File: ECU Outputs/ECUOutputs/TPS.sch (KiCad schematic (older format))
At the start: 22 parts, among them Q6 Q_NPN_BCE, Q7 Q_NPN_BCE, Q8 Q_PNP_BCE

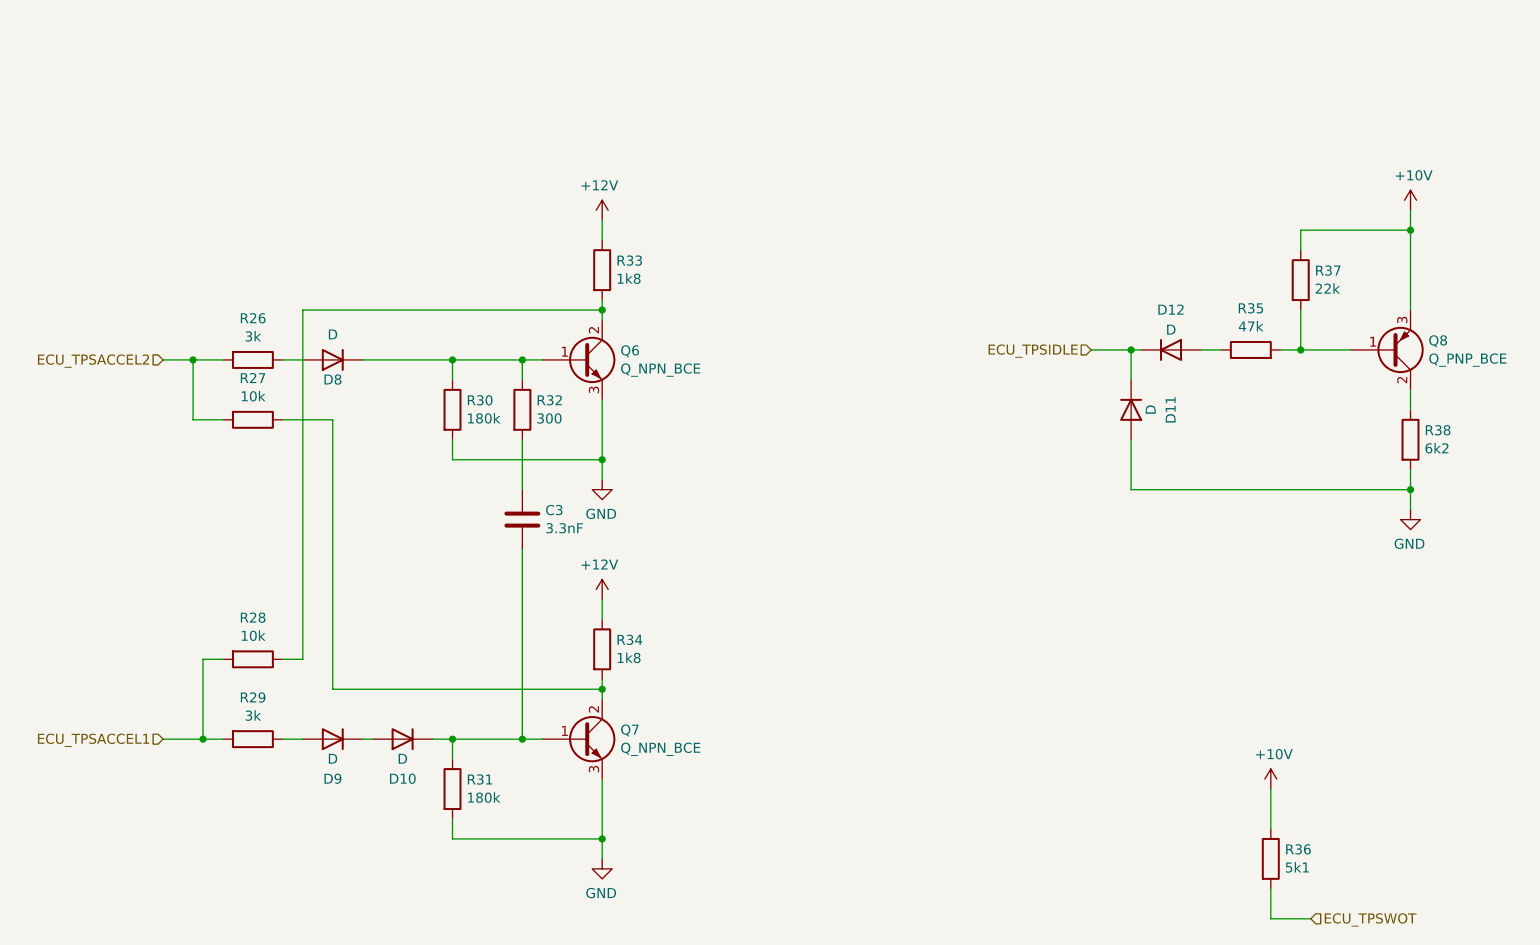
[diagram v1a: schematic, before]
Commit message: Updated manufacturer part numbers. Working on ECU outputs tester board.
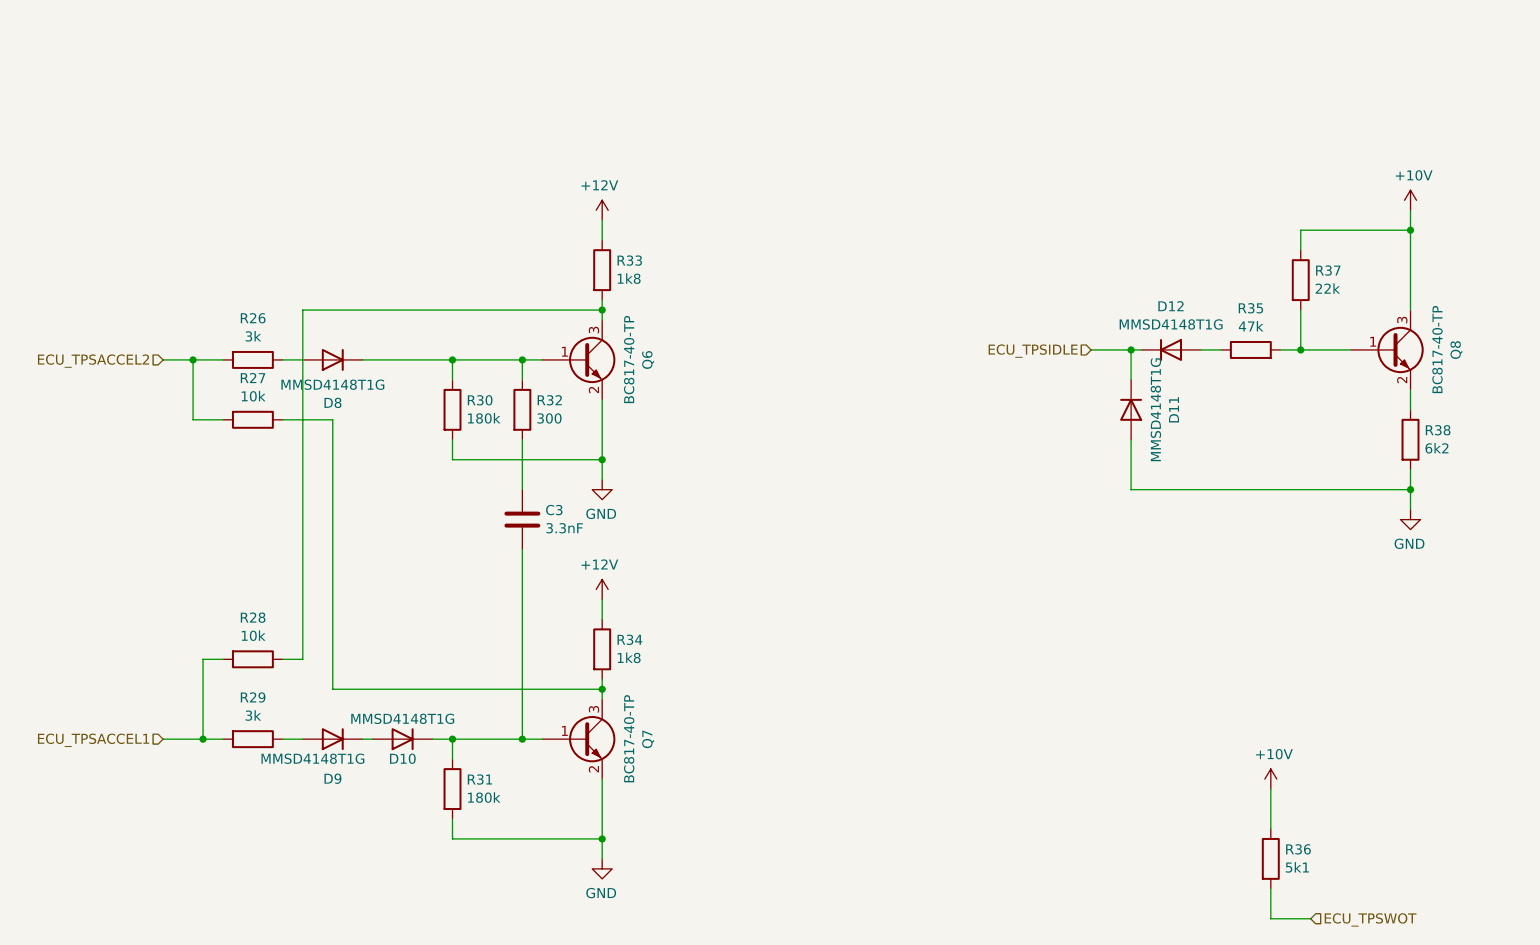
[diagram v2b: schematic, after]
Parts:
- removed Q6, Q7: Q_NPN_BCE, symbol Device:Q_NPN_BCE
- removed Q8: Q_PNP_BCE, symbol Device:Q_PNP_BCE
- added Q6, Q7, Q8: BC817-40-TP, Package_TO_SOT_SMD:SOT-23, symbol Device:Q_NPN_BEC
- C3: footprint (none) -> Capacitor_SMD:C_0805_2012Metric
- D10, D11, D12, D8, D9: value D -> MMSD4148T1G; footprint (none) -> Diode_SMD:D_SOD-123; manf# (none) -> MMSD4148T1G
- R26, R27, R28, R29, R30, R31, R32, R33, R34, R35, R36, R37, R38: footprint (none) -> Resistor_SMD:R_0805_2012Metric
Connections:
- net +10V: now also Q8.3 (C)
- net GND: now also Q6.2 (E), Q7.2 (E)
- net at R28.1, R33.2: now also Q6.3 (C)
- net at D8.1 (K), R30.1, R32.1: now also Q6.1 (B)
- net at R27.1, R34.2: now also Q7.3 (C)
- net at C3.2, D10.1 (K), R31.1: now also Q7.1 (B)
- net at R35.2, R37.2: now also Q8.1 (B)
- net at R38.1: now also Q8.2 (E)
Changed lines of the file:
@@
 F 0 "R33" H 4820 2396 50  0000 L CNN
 F 1 "1k8" H 4820 2305 50  0000 L CNN
-F 2 "" V 4680 2350 50  0001 C CNN
+F 2 "Resistor_SMD:R_0805_2012Metric" V 4680 2350 50  0001 C CNN
 F 3 "~" H 4750 2350 50  0001 C CNN
 	1    4750 2350
-	1    0    0    -1
-$EndComp
-$Comp
-L Device:Q_NPN_BCE Q?
-U 1 1 604AAF04
-P 4650 2800
-AR Path="/60469408/604AAF04" Ref="Q?"  Part="1"
-AR Path="/604A55C0/604AAF04" Ref="Q6"  Part="1"
-F 0 "Q6" H 4841 2846 50  0000 L CNN
-F 1 "Q_NPN_BCE" H 4841 2755 50  0000 L CNN
-F 2 "" H 4850 2900 50  0001 C CNN
-F 3 "~" H 4650 2800 50  0001 C CNN
-	1    4650 2800
 	1    0    0    -1
 $EndComp
@@
 F 0 "R30" H 4070 3096 50  0000 L CNN
 F 1 "180k" H 4070 3005 50  0000 L CNN
-F 2 "" V 3930 3050 50  0001 C CNN
+F 2 "Resistor_SMD:R_0805_2012Metric" V 3930 3050 50  0001 C CNN
 F 3 "~" H 4000 3050 50  0001 C CNN
 	1    4000 3050
@@
 F 0 "R32" H 4420 3096 50  0000 L CNN
 F 1 "300" H 4420 3005 50  0000 L CNN
-F 2 "" V 4280 3050 50  0001 C CNN
+F 2 "Resistor_SMD:R_0805_2012Metric" V 4280 3050 50  0001 C CNN
 F 3 "~" H 4350 3050 50  0001 C CNN
 	1    4350 3050
@@
 $EndComp
 Connection ~ 4000 2800
-$Comp
-L Device:D D?
-U 1 1 604AAF22
-P 3400 2800
-AR Path="/60469408/604AAF22" Ref="D?"  Part="1"
-AR Path="/604A55C0/604AAF22" Ref="D8"  Part="1"
-F 0 "D8" H 3400 2900 50  0000 C CNN
-F 1 "D" H 3400 2674 50  0000 C CNN
-F 2 "" H 3400 2800 50  0001 C CNN
-F 3 "~" H 3400 2800 50  0001 C CNN
-	1    3400 2800
-	-1   0    0    1
-$EndComp
 $Comp
 L Device:R R?
@@
 F 0 "R26" V 2793 2800 50  0000 C CNN
 F 1 "3k" V 2884 2800 50  0000 C CNN
-F 2 "" V 2930 2800 50  0001 C CNN
+F 2 "Resistor_SMD:R_0805_2012Metric" V 2930 2800 50  0001 C CNN
 F 3 "~" H 3000 2800 50  0001 C CNN
 	1    3000 2800
@@
 F 0 "R34" H 4820 4296 50  0000 L CNN
 F 1 "1k8" H 4820 4205 50  0000 L CNN
-F 2 "" V 4680 4250 50  0001 C CNN
+F 2 "Resistor_SMD:R_0805_2012Metric" V 4680 4250 50  0001 C CNN
 F 3 "~" H 4750 4250 50  0001 C CNN
 	1    4750 4250
-	1    0    0    -1
-$EndComp
-$Comp
-L Device:Q_NPN_BCE Q?
-U 1 1 604AAF45
-P 4650 4700
-AR Path="/60469408/604AAF45" Ref="Q?"  Part="1"
-AR Path="/604A55C0/604AAF45" Ref="Q7"  Part="1"
-F 0 "Q7" H 4841 4746 50  0000 L CNN
-F 1 "Q_NPN_BCE" H 4841 4655 50  0000 L CNN
-F 2 "" H 4850 4800 50  0001 C CNN
-F 3 "~" H 4650 4700 50  0001 C CNN
-	1    4650 4700
 	1    0    0    -1
 $EndComp
@@
 F 0 "R31" H 4070 4996 50  0000 L CNN
 F 1 "180k" H 4070 4905 50  0000 L CNN
-F 2 "" V 3930 4950 50  0001 C CNN
+F 2 "Resistor_SMD:R_0805_2012Metric" V 3930 4950 50  0001 C CNN
 F 3 "~" H 4000 4950 50  0001 C CNN
 	1    4000 4950
@@
 	4750 5200 4750 4900
 Connection ~ 4000 4700
-$Comp
-L Device:D D?
-U 1 1 604AAF5B
-P 3400 4700
-AR Path="/60469408/604AAF5B" Ref="D?"  Part="1"
-AR Path="/604A55C0/604AAF5B" Ref="D9"  Part="1"
-F 0 "D9" H 3400 4900 50  0000 C CNN
-F 1 "D" H 3400 4800 50  0000 C CNN
-F 2 "" H 3400 4700 50  0001 C CNN
-F 3 "~" H 3400 4700 50  0001 C CNN
-	1    3400 4700
-	-1   0    0    1
-$EndComp
 $Comp
 L Device:R R?
@@
 F 0 "R29" V 2793 4700 50  0000 C CNN
 F 1 "3k" V 2884 4700 50  0000 C CNN
-F 2 "" V 2930 4700 50  0001 C CNN
+F 2 "Resistor_SMD:R_0805_2012Metric" V 2930 4700 50  0001 C CNN
 F 3 "~" H 3000 4700 50  0001 C CNN
 	1    3000 4700
@@
 F 0 "C3" H 4465 3646 50  0000 L CNN
 F 1 "3.3nF" H 4465 3555 50  0000 L CNN
-F 2 "" H 4388 3450 50  0001 C CNN
+F 2 "Capacitor_SMD:C_0805_2012Metric" H 4388 3450 50  0001 C CNN
 F 3 "~" H 4350 3600 50  0001 C CNN
 	1    4350 3600
@@
 F 0 "R28" V 2793 4300 50  0000 C CNN
 F 1 "10k" V 2884 4300 50  0000 C CNN
-F 2 "" V 2930 4300 50  0001 C CNN
+F 2 "Resistor_SMD:R_0805_2012Metric" V 2930 4300 50  0001 C CNN
 F 3 "~" H 3000 4300 50  0001 C CNN
 	1    3000 4300
@@
 F 0 "R27" V 2793 3100 50  0000 C CNN
 F 1 "10k" V 2884 3100 50  0000 C CNN
-F 2 "" V 2930 3100 50  0001 C CNN
+F 2 "Resistor_SMD:R_0805_2012Metric" V 2930 3100 50  0001 C CNN
 F 3 "~" H 3000 3100 50  0001 C CNN
 	1    3000 3100
@@
 Wire Wire Line
 	4750 2550 4750 2600
-$Comp
-L Device:D D?
-U 1 1 604AD283
-P 3750 4700
-AR Path="/60469408/604AD283" Ref="D?"  Part="1"
-AR Path="/604A55C0/604AD283" Ref="D10"  Part="1"
-F 0 "D10" H 3750 4900 50  0000 C CNN
-F 1 "D" H 3750 4800 50  0000 C CNN
-F 2 "" H 3750 4700 50  0001 C CNN
-F 3 "~" H 3750 4700 50  0001 C CNN
-	1    3750 4700
-	-1   0    0    1
-$EndComp
 Wire Wire Line
 	3900 4700 4000 4700
@@
 Text HLabel 7200 2750 0    50   Input ~ 0
 ECU_TPSIDLE
-$Comp
-L Device:D D?
-U 1 1 604CC7C0
-P 7600 2750
-AR Path="/60469408/604CC7C0" Ref="D?"  Part="1"
-AR Path="/604A55C0/604CC7C0" Ref="D12"  Part="1"
-F 0 "D12" H 7600 2950 50  0000 C CNN
-F 1 "D" H 7600 2850 50  0000 C CNN
-F 2 "" H 7600 2750 50  0001 C CNN
-F 3 "~" H 7600 2750 50  0001 C CNN
-	1    7600 2750
-	1    0    0    -1
-$EndComp
 $Comp
 L Device:R R?
@@
 F 0 "R35" V 8207 2750 50  0000 C CNN
 F 1 "47k" V 8116 2750 50  0000 C CNN
-F 2 "" V 7930 2750 50  0001 C CNN
+F 2 "Resistor_SMD:R_0805_2012Metric" V 7930 2750 50  0001 C CNN
 F 3 "~" H 8000 2750 50  0001 C CNN
 	1    8000 2750
@@
 Wire Wire Line
 	7750 2750 7850 2750
-$Comp
-L Device:Q_PNP_BCE Q8
-U 1 1 604CEFC7
-P 8700 2750
-F 0 "Q8" H 8890 2704 50  0000 L CNN
-F 1 "Q_PNP_BCE" H 8890 2795 50  0000 L CNN
-F 2 "" H 8900 2850 50  0001 C CNN
-F 3 "~" H 8700 2750 50  0001 C CNN
-	1    8700 2750
-	1    0    0    1
-$EndComp
 $Comp
 L Device:R R?
@@
 F 0 "R37" H 8320 2446 50  0000 L CNN
 F 1 "22k" H 8320 2355 50  0000 L CNN
-F 2 "" V 8180 2400 50  0001 C CNN
+F 2 "Resistor_SMD:R_0805_2012Metric" V 8180 2400 50  0001 C CNN
 F 3 "~" H 8250 2400 50  0001 C CNN
 	1    8250 2400
@@
 F 0 "R38" H 8870 3246 50  0000 L CNN
 F 1 "6k2" H 8870 3155 50  0000 L CNN
-F 2 "" V 8730 3200 50  0001 C CNN
+F 2 "Resistor_SMD:R_0805_2012Metric" V 8730 3200 50  0001 C CNN
 F 3 "~" H 8800 3200 50  0001 C CNN
 	1    8800 3200
 	1    0    0    -1
-$EndComp
-$Comp
-L Device:D D?
-U 1 1 604D47CA
-P 7400 3050
-AR Path="/60469408/604D47CA" Ref="D?"  Part="1"
-AR Path="/604A55C0/604D47CA" Ref="D11"  Part="1"
-F 0 "D11" H 7400 3250 50  0000 C CNN
-F 1 "D" H 7400 3150 50  0000 C CNN
-F 2 "" H 7400 3050 50  0001 C CNN
-F 3 "~" H 7400 3050 50  0001 C CNN
-	1    7400 3050
-	0    1    1    0
 $EndComp
 Wire Wire Line
@@
 F 0 "R36" H 8170 5346 50  0000 L CNN
 F 1 "5k1" H 8170 5255 50  0000 L CNN
-F 2 "" V 8030 5300 50  0001 C CNN
+F 2 "Resistor_SMD:R_0805_2012Metric" V 8030 5300 50  0001 C CNN
 F 3 "~" H 8100 5300 50  0001 C CNN
 	1    8100 5300
@@
 Wire Wire Line
 	8100 4950 8100 5150
+$Comp
+L Device:Q_NPN_BEC Q?
+U 1 1 6050DF73
+P 4650 2800
+AR Path="/6050DF73" Ref="Q?"  Part="1"
+AR Path="/604A55C0/6050DF73" Ref="Q6"  Part="1"
+F 0 "Q6" V 4978 2800 50  0000 C CNN
+F 1 "BC817-40-TP" V 4887 2800 50  0000 C CNN
+F 2 "Package_TO_SOT_SMD:SOT-23" H 4850 2900 50  0001 C CNN
+F 3 "~" H 4650 2800 50  0001 C CNN
+F 4 "BC817-40-TP" V 4650 2800 50  0001 C CNN "manf#"
+	1    4650 2800
+	1    0    0    -1
+$EndComp
+$Comp
+L Device:Q_NPN_BEC Q?
+U 1 1 6050F1C9
+P 4650 4700
+AR Path="/6050F1C9" Ref="Q?"  Part="1"
+AR Path="/604A55C0/6050F1C9" Ref="Q7"  Part="1"
+F 0 "Q7" V 4978 4700 50  0000 C CNN
+F 1 "BC817-40-TP" V 4887 4700 50  0000 C CNN
+F 2 "Package_TO_SOT_SMD:SOT-23" H 4850 4800 50  0001 C CNN
+F 3 "~" H 4650 4700 50  0001 C CNN
+F 4 "BC817-40-TP" V 4650 4700 50  0001 C CNN "manf#"
+	1    4650 4700
+	1    0    0    -1
+$EndComp
+$Comp
+L Device:Q_NPN_BEC Q?
+U 1 1 6050F8A0
+P 8700 2750
+AR Path="/6050F8A0" Ref="Q?"  Part="1"
+AR Path="/604A55C0/6050F8A0" Ref="Q8"  Part="1"
+F 0 "Q8" V 9028 2750 50  0000 C CNN
+F 1 "BC817-40-TP" V 8937 2750 50  0000 C CNN
+F 2 "Package_TO_SOT_SMD:SOT-23" H 8900 2850 50  0001 C CNN
+F 3 "~" H 8700 2750 50  0001 C CNN
+F 4 "BC817-40-TP" V 8700 2750 50  0001 C CNN "manf#"
+	1    8700 2750
+	1    0    0    -1
+$EndComp
+$Comp
+L Device:D D?
+U 1 1 6052AE44
+P 3400 2800
+AR Path="/6052AE44" Ref="D?"  Part="1"
+AR Path="/604A55C0/6052AE44" Ref="D8"  Part="1"
+F 0 "D8" H 3400 3017 50  0000 C CNN
+F 1 "MMSD4148T1G" H 3400 2926 50  0000 C CNN
+F 2 "Diode_SMD:D_SOD-123" H 3400 2800 50  0001 C CNN
+F 3 "~" H 3400 2800 50  0001 C CNN
+F 4 "MMSD4148T1G" H 3400 2800 50  0001 C CNN "manf#"
+	1    3400 2800
+	-1   0    0    1
+$EndComp
 Wire Wire Line
 	3250 2550 3250 4300
+$Comp
+L Device:D D?
+U 1 1 6052BF0A
+P 3400 4700
+AR Path="/6052BF0A" Ref="D?"  Part="1"
+AR Path="/604A55C0/6052BF0A" Ref="D9"  Part="1"
+F 0 "D9" H 3400 4900 50  0000 C CNN
+F 1 "MMSD4148T1G" H 3500 4800 50  0000 C CNN
+F 2 "Diode_SMD:D_SOD-123" H 3400 4700 50  0001 C CNN
+F 3 "~" H 3400 4700 50  0001 C CNN
+F 4 "MMSD4148T1G" H 3400 4700 50  0001 C CNN "manf#"
+	1    3400 4700
+	-1   0    0    1
+$EndComp
+$Comp
+L Device:D D?
+U 1 1 6052CCA7
+P 3750 4700
+AR Path="/6052CCA7" Ref="D?"  Part="1"
+AR Path="/604A55C0/6052CCA7" Ref="D10"  Part="1"
+F 0 "D10" H 3750 4800 50  0000 C CNN
+F 1 "MMSD4148T1G" H 3750 4600 50  0000 C CNN
+F 2 "Diode_SMD:D_SOD-123" H 3750 4700 50  0001 C CNN
+F 3 "~" H 3750 4700 50  0001 C CNN
+F 4 "MMSD4148T1G" H 3750 4700 50  0001 C CNN "manf#"
+	1    3750 4700
+	-1   0    0    1
+$EndComp
+$Comp
+L Device:D D?
+U 1 1 6052D930
+P 7400 3050
+AR Path="/6052D930" Ref="D?"  Part="1"
+AR Path="/604A55C0/6052D930" Ref="D11"  Part="1"
+F 0 "D11" H 7400 3267 50  0000 C CNN
+F 1 "MMSD4148T1G" H 7400 3176 50  0000 C CNN
+F 2 "Diode_SMD:D_SOD-123" H 7400 3050 50  0001 C CNN
+F 3 "~" H 7400 3050 50  0001 C CNN
+F 4 "MMSD4148T1G" H 7400 3050 50  0001 C CNN "manf#"
+	1    7400 3050
+	0    1    1    0
+$EndComp
+$Comp
+L Device:D D?
+U 1 1 6052E5D7
+P 7600 2750
+AR Path="/6052E5D7" Ref="D?"  Part="1"
+AR Path="/604A55C0/6052E5D7" Ref="D12"  Part="1"
+F 0 "D12" H 7600 2967 50  0000 C CNN
+F 1 "MMSD4148T1G" H 7600 2876 50  0000 C CNN
+F 2 "Diode_SMD:D_SOD-123" H 7600 2750 50  0001 C CNN
+F 3 "~" H 7600 2750 50  0001 C CNN
+F 4 "MMSD4148T1G" H 7600 2750 50  0001 C CNN "manf#"
+	1    7600 2750
+	1    0    0    -1
+$EndComp
 $EndSCHEMATC
